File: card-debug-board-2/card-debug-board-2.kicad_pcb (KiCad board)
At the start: 2 copper layers, 62 x 30 mm, 26 parts, among them J1 J-TE-Debug-2-1734592-0, J2 Conn_01x05, J5 USB_A, J6 USB_B_Micro, SW1 SW_DIP_x01, SW2 C&K PCM13SMTR, SW3 Omron B3F-1000, SW4 SW_DIP_x01, U1 MIC5205-3.3YM5

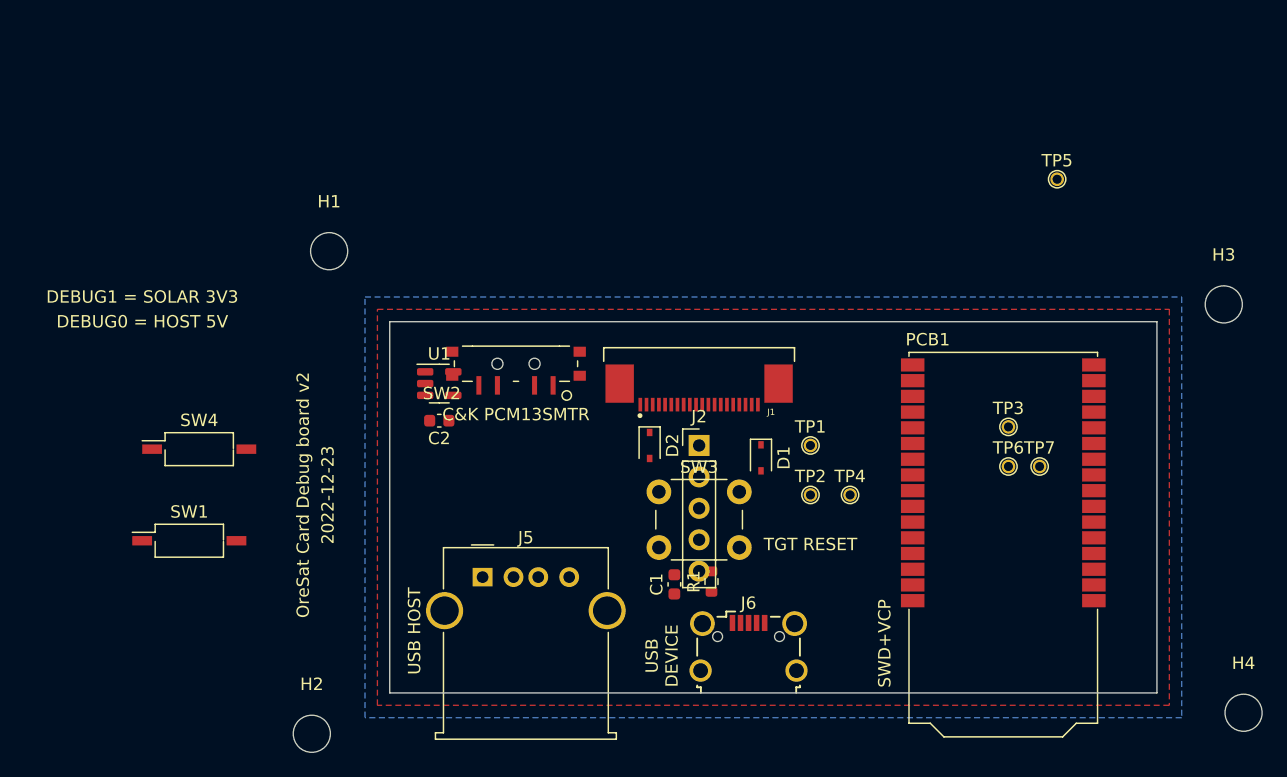
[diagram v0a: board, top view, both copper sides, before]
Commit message: Completed rough draft layout of Card Debug Board v2.
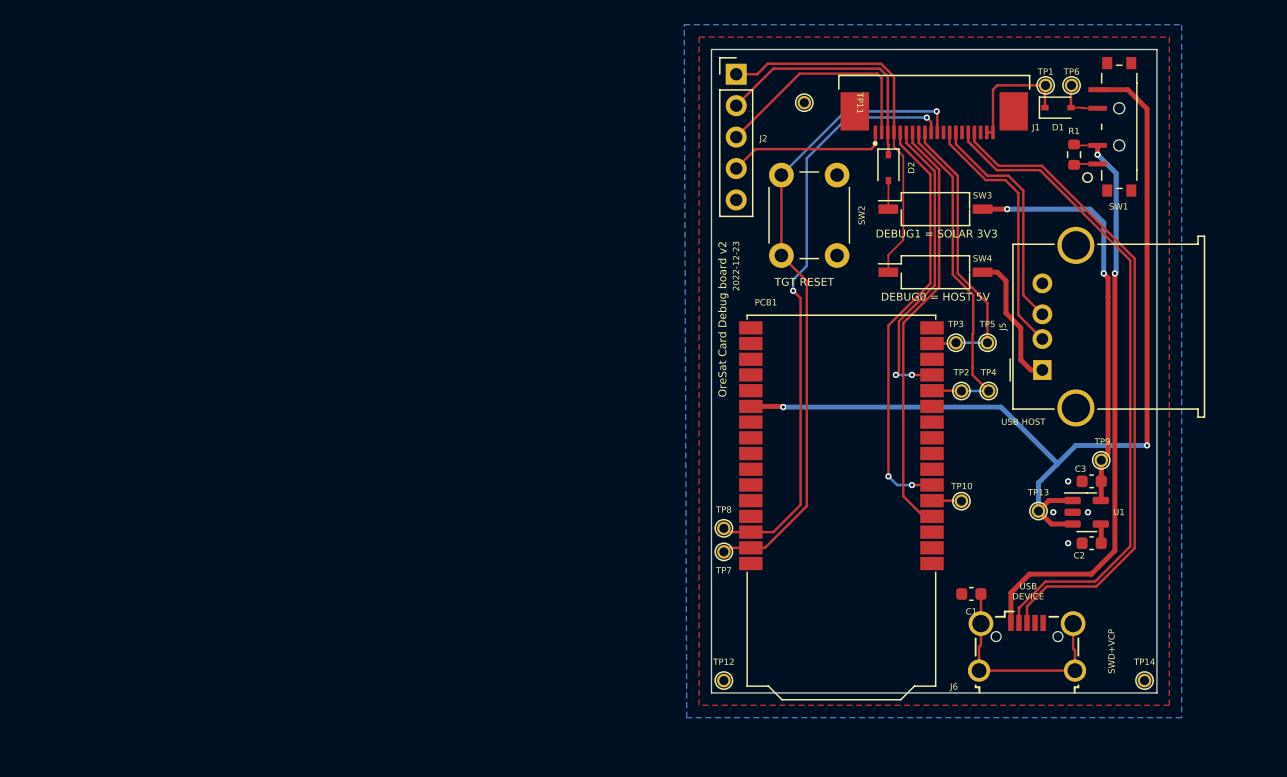
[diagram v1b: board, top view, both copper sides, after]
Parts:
- removed H1, H2, H3, H4: MountingHole, MountingHole:MountingHole_3mm
- added C3: 2.2u, Capacitor_SMD:C_0603_1608Metric, F.Cu at (156.7, 82.9)
- added TP10: TestPoint-MinTH, oresat-misc:TestPoint-MinTH, F.Cu at (146.2, 84.5)
- added TP11: TestPoint-MinTH, oresat-misc:TestPoint-MinTH, F.Cu at (133.5, 52.3)
- added TP12: TestPoint-MinTH, oresat-misc:TestPoint-MinTH, F.Cu at (127.0, 99.0)
- added TP13: TestPoint-MinTH, oresat-misc:TestPoint-MinTH, F.Cu at (152.4, 85.3)
- added TP14: TestPoint-MinTH, oresat-misc:TestPoint-MinTH, F.Cu at (161.0, 99.0)
- added TP8: TestPoint-MinTH, oresat-misc:TestPoint-MinTH, F.Cu at (127.0, 86.7)
- added TP9: TestPoint-MinTH, oresat-misc:TestPoint-MinTH, F.Cu at (157.5, 81.2)
- C2: value ??? -> 470p
- D1, D2: value D_Schottky_Small_Filled -> ZLLS410TA
- J1: value J-TE-Debug-2-1734592-0 -> 2-1734592-0
- J5: value USB_A -> 0676430910
- J6: value USB_B_Micro -> 629105150521
- SW1: value SW_DIP_x01 -> PCM13SMTR; footprint Button_Switch_SMD:SW_DIP_SPSTx01_Slide_Copal_CHS-01B_W7.62mm_P1.27mm -> oresat-misc:SW-CK-PCM13SMTR
- SW2: value C&K PCM13SMTR -> B3F-1000; footprint oresat-misc:SW-CK-PCM13SMTR -> Button_Switch_THT:SW_PUSH_6mm
- SW3: value Omron B3F-1000 -> CFS-0103TB; footprint Button_Switch_THT:SW_PUSH_6mm -> Button_Switch_SMD:SW_DIP_SPSTx01_Slide_Copal_CHS-01B_W7.62mm_P1.27mm
- SW4: value SW_DIP_x01 -> CFS-0103TB
- moved SW1 82.3 mm to (158.9, 54.2), turned to 90 degrees
- moved SW4 61.2 mm to (144.1, 66.0)
- moved C2 53.6 mm to (156.7, 87.9)
- moved U1 53.3 mm to (156.3, 85.4)
- moved J5 48.2 mm to (152.7, 73.9), turned to 90 degrees
- moved R1 45.3 mm to (155.3, 56.5), turned to -90 degrees
- moved D1 37.1 mm to (154.0, 52.7), turned to 0 degrees
- moved TP1 34.8 mm to (153.0, 50.9)
- moved SW3 32.0 mm to (144.1, 60.9)
- moved TP6 31.2 mm to (155.1, 50.9)
- moved J2 30.1 mm to (128.0, 50.0)
- moved SW2 30.1 mm to (136.2, 58.1), turned to -90 degrees
- moved D2 29.6 mm to (140.3, 57.5)
- moved J1 29.1 mm to (144.0, 53.0)
- moved TP7 26.4 mm to (127.0, 88.6), turned to 180 degrees
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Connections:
- net Net-(D2-Pad1) renamed /DEBUG1/SOLAR3V3
- net Net-(J1-Pad17) renamed /DEBUG0/5VUSBHOST
- net Net-(J1-Pad19) renamed /DEBUG2
- net Net-(J1-Pad20) renamed /DEBUG3
- J2 pad 5: unconnected-(J2-Pad5) -> GND
- SW1 pad 1: Net-(D2-Pad2) -> Net-(R1-Pad2)
- SW1 pad 2: +3.3V -> Net-(J6-Pad1)
- SW2 pad 1: Net-(R1-Pad2) -> GND
- SW2 pad 2: Net-(J6-Pad1) -> Net-(J1-Pad10)
- SW3 pad 1: GND -> Net-(D2-Pad2)
- SW3 pad 2: Net-(J1-Pad10) -> +3.3V
- TP2 pad 1: Net-(J1-Pad12) -> Net-(J1-Pad13)
- TP3 pad 1: Net-(J1-Pad13) -> Net-(J1-Pad12)
- TP4 pad 1: Net-(J1-Pad12) -> Net-(J1-Pad13)
- TP5 pad 1: Net-(D1-Pad2) -> Net-(J1-Pad12)
- TP6 pad 1: Net-(J1-Pad13) -> Net-(D1-Pad2)
- TP7 pad 1: Net-(PCB1-Pad5) -> Net-(J1-Pad10)
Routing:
- net +5V: track 0.00 -> 77.1 mm, vias 0 -> 2
- net Net-(J1-Pad5): track 0.00 -> 53.2 mm
- net Net-(J1-Pad4): track 0.00 -> 53.0 mm
- net Net-(J1-Pad10): track 0.00 -> 52.2 mm, vias 0 -> 1
- net Net-(J1-Pad11): track 0.00 -> 48.4 mm, vias 0 -> 2
- net Net-(J6-Pad1): track 0.00 -> 47.6 mm, vias 0 -> 2
- net Net-(J1-Pad14): track 0.00 -> 34.5 mm
- net Net-(J1-Pad16): track 0.00 -> 34.0 mm, vias 0 -> 2
- net +3.3V: track 0.00 -> 33.1 mm, vias 0 -> 2
- net /DEBUG0/5VUSBHOST: track 0.00 -> 30.1 mm
- net Net-(J1-Pad13): track 0.00 -> 27.9 mm
- net Net-(J1-Pad15): track 0.00 -> 24.8 mm, vias 0 -> 2
- net Net-(J1-Pad12): track 0.00 -> 23.6 mm
- net Net-(J1-Pad8): track 0.00 -> 20.7 mm
- net /DEBUG1/SOLAR3V3: track 0.00 -> 20.1 mm
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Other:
- board size 62 x 30 mm -> 36 x 52 mm

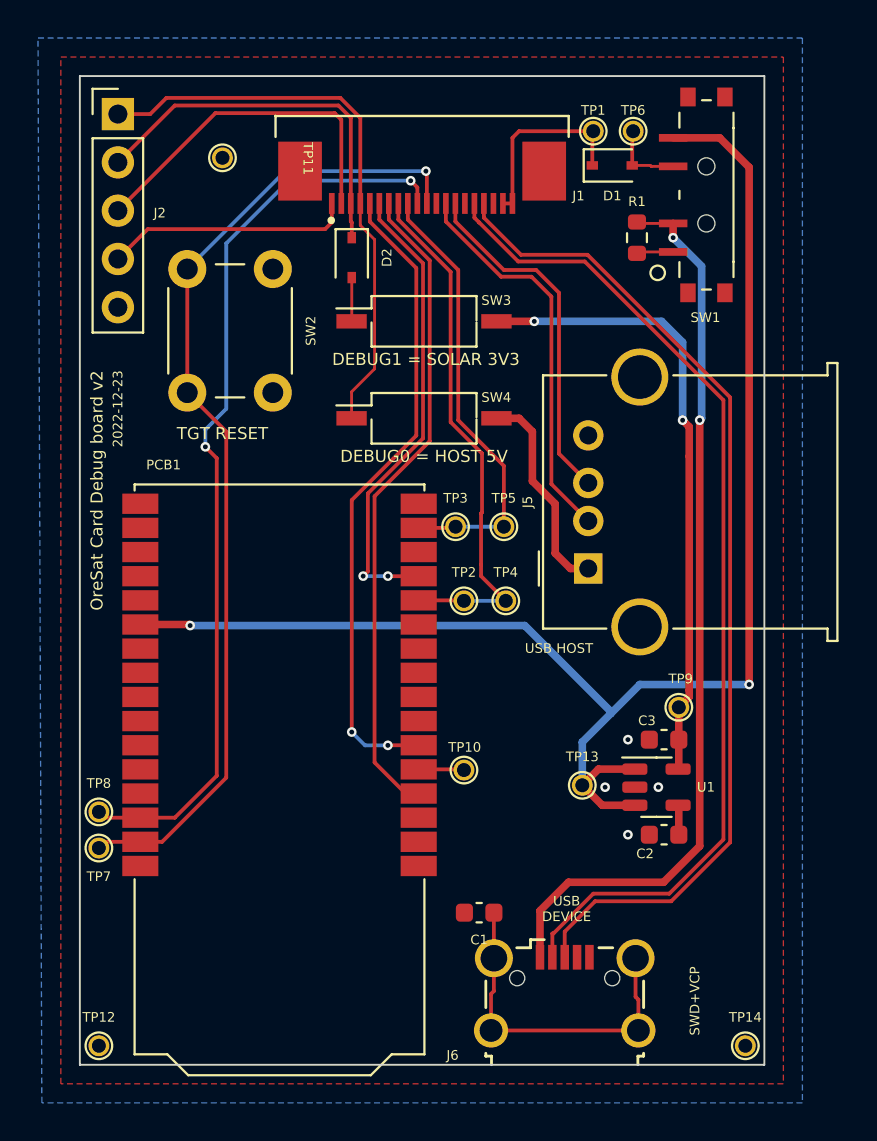
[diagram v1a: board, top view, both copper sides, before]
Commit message: Polish on the schematic and layout, including MFR/MPN additions, datasheet links, ground stitching, better text descriptions, etc.
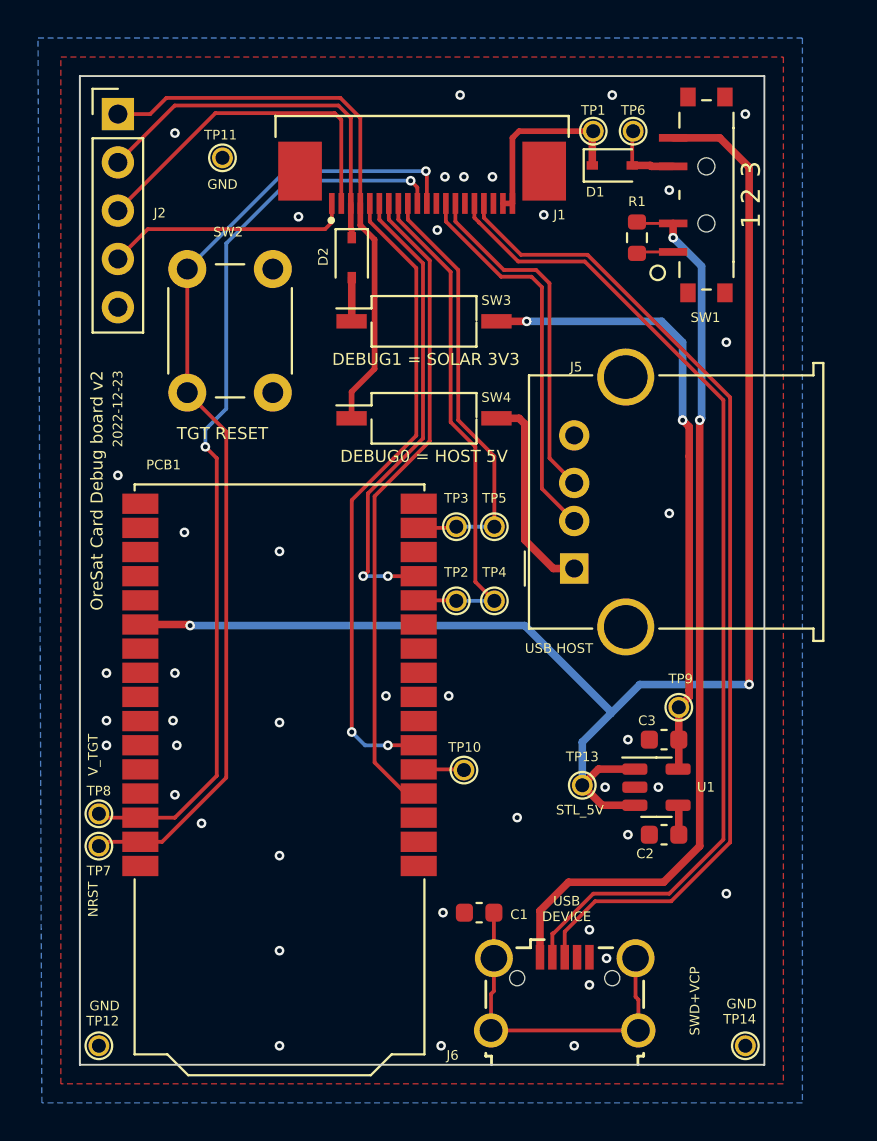
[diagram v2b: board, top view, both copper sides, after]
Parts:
- moved J5 0.74 mm to (152.0, 73.9)
- moved TP4 0.60 mm to (147.8, 75.6)
- moved TP5 0.50 mm to (147.8, 71.7)
- moved TP2 0.40 mm to (145.8, 75.6)
- moved TP7 0.10 mm to (127.0, 88.5)
- moved TP8 0.10 mm to (127.0, 86.8)
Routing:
- net Net-(J1-Pad13): track 27.9 -> 27.0 mm
- net Net-(J1-Pad12): track 23.6 -> 22.9 mm
- net GND: vias 4 -> 42
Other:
- board text added: "1"
- board text added: "1: VUSB through 10k for Octavo USB 2: VUSB straight to power Octavo 3: STLINK VUSB to VBUSP"
- board text added: "2"
- board text added: "3"
- board text added: "GND"
- board text added: "NRST"
- board text added: "STL_5V"
- board text added: "V_TGT"
